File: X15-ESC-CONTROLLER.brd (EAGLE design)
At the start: 51.6 x 34.2 mm, 27 parts, among them IC1 OP-AMP, J1 3V3 -SWCLK-GND-SWDIO- NRST, Y1 ECS-80-S-4X

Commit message: First finished version
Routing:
- net GND: track 161.2 -> 160.6 mm
- net TIM2_CH2: track 37.2 -> 36.6 mm

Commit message: Final Version 2
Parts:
- moved J2 1.07 mm to (19.9, 3.15)
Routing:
- net TIM3_CH3: track 33.8 -> 32.2 mm
- net ADC_IN4: track 23.5 -> 22.0 mm
- net TIM3_CH4: track 35.2 -> 33.9 mm
- net TIM1_CH1: track 41.9 -> 43.1 mm
- net TIM16_CH1: track 37.5 -> 36.5 mm

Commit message: Update Parts Library
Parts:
- D1: device LED, 0805:0805 -> X15-ESC-Controller-Parts-Library:0805
- U$7: device OTHER, Push button - FSM2JMTR:DISCRETECOMPONENTS_SW_2512 -> X15-ESC-Controller-Parts-Library:DISCRETECOMPONENTS_SW_2512
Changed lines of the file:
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@@
 <attribute name="VALUE" x="8.2296" y="10.2108" size="0.6096" layer="28" font="vector" ratio="20" rot="MR180"/>
 </element>
-<element name="U$7" library="OTHER, Push button - FSM2JMTR" package="DISCRETECOMPONENTS_SW_2512" package3d_urn="urn:adsk.eagle:package:24384574/2" value="" x="4.445" y="8.382" smashed="yes" rot="R90">
+<element name="U$7" library="X15-ESC-Controller-Parts-Library" package="DISCRETECOMPONENTS_SW_2512" package3d_urn="urn:adsk.eagle:package:24384574/2" value="" x="4.445" y="8.382" smashed="yes" rot="R90">
 <attribute name="NAME" x="2.54" y="8.382" size="1.27" layer="25" rot="R90" align="bottom-center"/>
 <attribute name="VALUE" x="6.35" y="8.382" size="1.27" layer="27" rot="R90" align="top-center"/>
 </element>
-<element name="D1" library="LED, 0805" package="0805" value="COLOR" x="2.667" y="14.6812" smashed="yes">
+<element name="D1" library="X15-ESC-Controller-Parts-Library" package="0805" value="COLOR" x="2.667" y="14.6812" smashed="yes">
 <attribute name="NAME" x="2.667" y="15.5702" size="0.6096" layer="25" font="vector" ratio="20" align="bottom-center"/>
 <attribute name="VALUE" x="2.667" y="13.7922" size="0.6096" layer="27" font="vector" ratio="20" align="top-center"/>

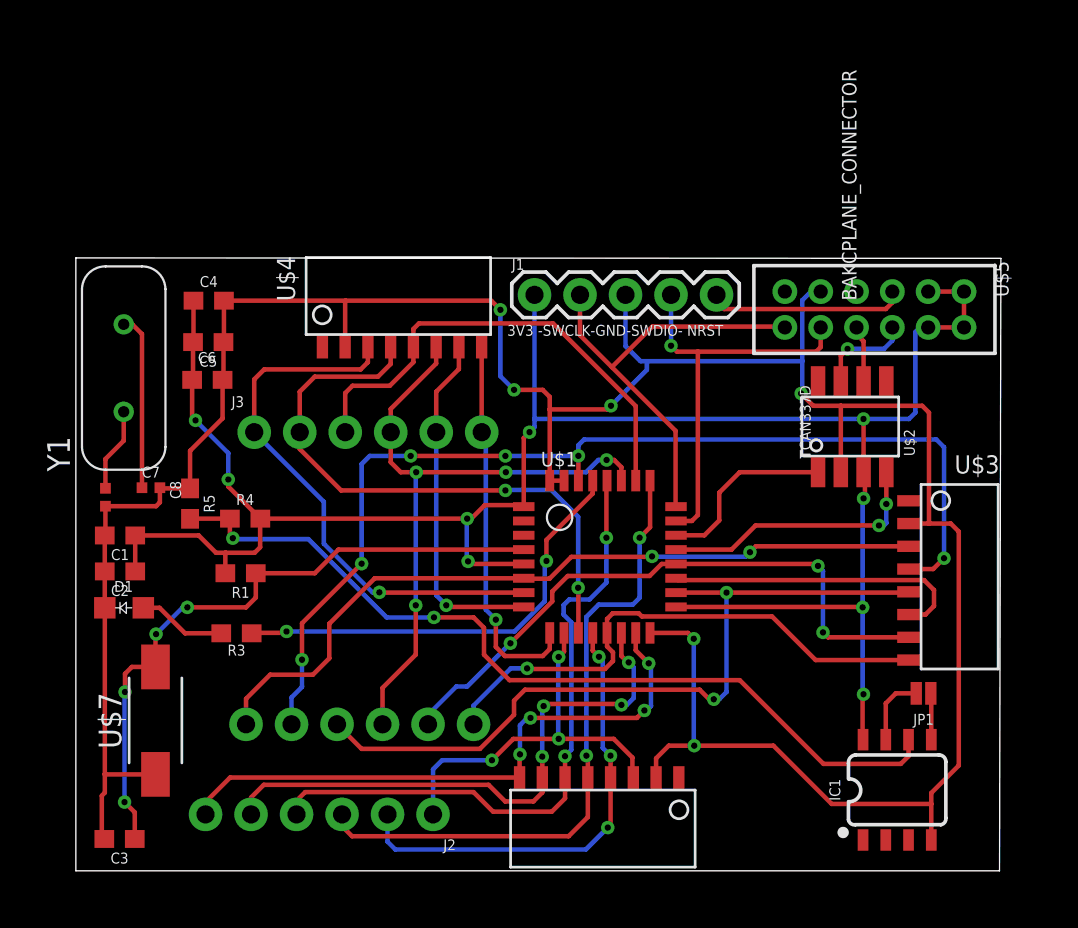
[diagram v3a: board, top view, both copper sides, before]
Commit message: Fix some traces with polygons
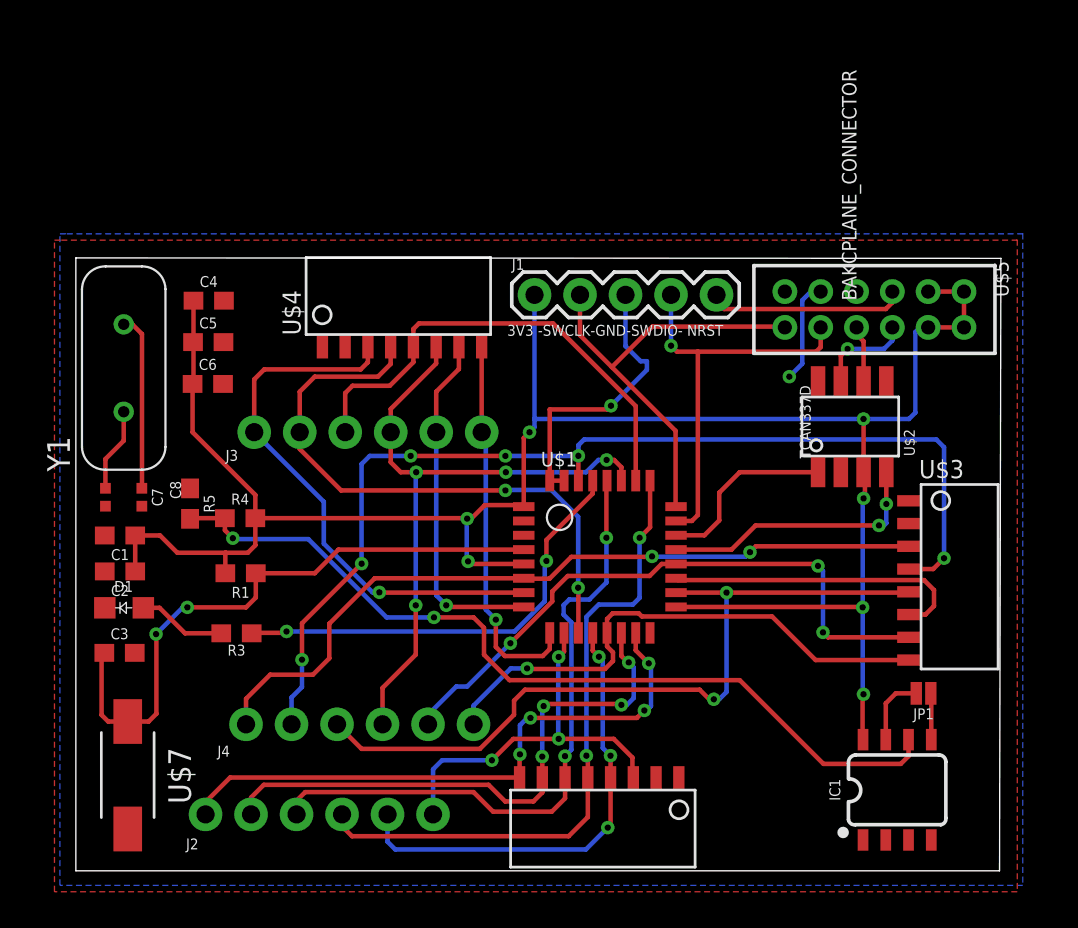
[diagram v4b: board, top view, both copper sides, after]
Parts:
- moved C3 10.4 mm to (2.44, 12.2), turned to 0 degrees
- moved U$7 3.42 mm to (2.90, 5.33)
- moved C7 0.74 mm to (3.68, 20.9), turned to 270 degrees
- moved R4 0.28 mm to (9.17, 19.7)
- moved C6 0.23 mm to (7.37, 27.2)
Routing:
- net GND: track 160.6 -> 21.8 mm, vias 6 -> 2
- net N$2: track 36.4 -> 34.7 mm, vias 4 -> 2
- net +3V3: track 119.9 -> 119.8 mm, vias 9 -> 7
- added copper zone on layer 1, net GND
- added copper zone on layer 16, net GND

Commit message: Add 3.3V testing LED
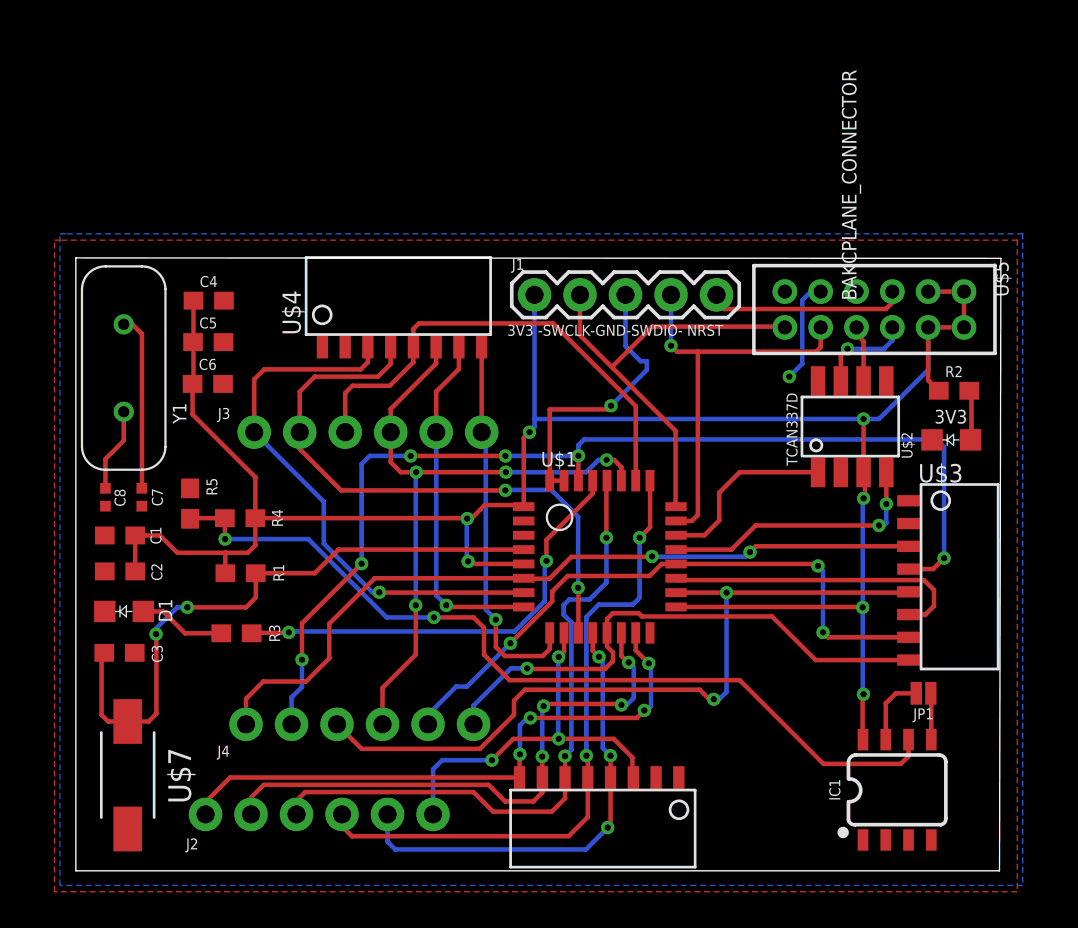
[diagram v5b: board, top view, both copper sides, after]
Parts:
- added 3V3: COLOR, X15-ESC-Controller-Parts-Library:0805
- added R2: 150, SparkFun-Resistors:0603
- moved D1 0.20 mm to (2.67, 14.5)
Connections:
- new net N$1: 3V3.A, R2.2
- net +3V3: now also R2.1
- net GND: now also 3V3.C
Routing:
- net N$1: track 0.00 -> 2.82 mm
- net +3V3: track 119.8 -> 122.3 mm

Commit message: Update .brd file
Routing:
- net GND: track 21.8 -> 11.8 mm
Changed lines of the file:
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@@
 </element>
 <element name="3V3" library="X15-ESC-Controller-Parts-Library" package="0805" value="COLOR" x="48.8442" y="24.0538" smashed="yes">
-<attribute name="NAME" x="48.8442" y="24.9682" size="0.762" layer="25" font="vector" ratio="20" align="bottom-center"/>
+<attribute name="NAME" x="48.8442" y="24.9682" size="0.6096" layer="25" font="vector" ratio="20" align="bottom-center"/>
 <attribute name="VALUE" x="49.8856" y="23.3426" size="0.6096" layer="27" font="vector" ratio="20" align="top-center"/>
 </element>
@@
 <contactref element="D1" pad="C"/>
 <via x="39.8272" y="27.5844" extent="1-16" drill="0.35"/>
-<wire x1="30.6832" y1="32.152" x2="30.6832" y2="29.2862" width="0.254" layer="16"/>
-<wire x1="31.5214" y1="28.448" x2="31.877" y2="28.448" width="0.254" layer="16"/>
-<wire x1="31.5214" y1="28.448" x2="30.6832" y2="29.2862" width="0.254" layer="16"/>
 <wire x1="26.4526" y1="21.7798" x2="27.2526" y2="21.7798" width="0.254" layer="1"/>
-<wire x1="26.4526" y1="25.7556" x2="26.4526" y2="21.7798" width="0.254" layer="1"/>
-<wire x1="26.4526" y1="25.7556" x2="29.6672" y2="25.7556" width="0.254" layer="1"/>
 <wire x1="41.5776" y1="32.3342" x2="41.0346" y2="32.3342" width="0.254" layer="16"/>
 <wire x1="40.552" y1="31.8516" x2="40.552" y2="28.3092" width="0.254" layer="16"/>
 <wire x1="41.0346" y1="32.3342" x2="40.552" y2="31.8516" width="0.254" layer="16"/>
 <wire x1="40.552" y1="28.3092" x2="39.8272" y2="27.5844" width="0.254" layer="16"/>
-<wire x1="31.877" y1="27.9654" x2="31.877" y2="28.448" width="0.254" layer="16"/>
-<wire x1="29.872421875" y1="25.960821875" x2="31.877" y2="27.9654" width="0.254" layer="16"/>
-<wire x1="29.6672" y1="25.7556" x2="29.872421875" y2="25.960821875" width="0.254" layer="1"/>
-<via x="29.872421875" y="25.960821875" extent="1-16" drill="0.35"/>
+<wire x1="26.4526" y1="21.7798" x2="26.4526" y2="26.94224375" width="0.254" layer="1"/>
+<wire x1="26.4526" y1="26.94224375" x2="26.443421875" y2="26.951421875" width="0.254" layer="1"/>
+<via x="26.443421875" y="26.951421875" extent="1-16" drill="0.35"/>
 <polygon width="0.1524" layer="1" isolate="0.2032">
 <vertex x="-0.8128" y="35.2044"/>

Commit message: Complete Board
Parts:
- JP1: value JUMPER-SMT_2_NO_NO-SILK -> JUMPER-SMT
- U$3, U$4, U$6: device X15-ESC-Controller-Parts-Library:JST_8_PIN -> X15-ESC-Controller-Parts-Library:8PIN_CONNECTOR
- moved U$4 10.2 mm to (12.4, 28.4), turned to 0 degrees
- moved U$6 9.39 mm to (34.1, 5.82), turned to 180 degrees
- moved U$3 8.28 mm to (45.8, 20.0), turned to 270 degrees
- moved IC1 7.17 mm to (38.7, 4.70)
- moved JP1 4.88 mm to (42.4, 9.91), turned to 90 degrees
- moved R4 2.27 mm to (7.11, 18.7), turned to 180 degrees
- moved R3 2.22 mm to (7.11, 14.5)
- moved J4 2.21 mm to (7.29, 8.13)
- moved R1 2.09 mm to (7.11, 16.7)
- moved R5 0.83 mm to (7.11, 20.9), turned to 0 degrees
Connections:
- net ADC_IN0: now also U$3.1; no longer U$3.3
- net ADC_IN1: now also U$4.1; no longer U$4.3
- net ADC_IN4: now also U$6.1; no longer U$6.3
- net TIM16_CH1: now also U$6.4; no longer U$6.5
- net TIM17_CH1: now also U$3.7; no longer U$3.8
- net TIM1_CH1: now also U$3.4; no longer U$3.5
- net TIM1_CH2: now also U$3.5; no longer U$3.6
- net TIM1_CH3: now also U$3.6; no longer U$3.7
- net TIM2_CH1: now also U$4.4; no longer U$4.5
- net TIM2_CH2: now also U$4.5; no longer U$4.6
- net TIM2_CH3: now also U$4.6; no longer U$4.7
- net TIM2_CH4: now also U$4.7; no longer U$4.8
- net TIM3_CH2: now also U$6.5; no longer U$6.6
- net TIM3_CH3: now also U$6.6; no longer U$6.7
- net TIM3_CH4: now also U$6.7; no longer U$6.8
- net TLM_1: now also U$3.8; no longer U$3.4
- net TLM_2: now also U$4.8; no longer U$4.4
- net TLM_3: now also U$6.8; no longer U$6.4
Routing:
- net TIM3_CH2: track 36.4 -> 53.2 mm, vias 2 -> 1
- net +3V3: track 122.3 -> 108.9 mm, vias 7 -> 6
- net ADC_IN4: track 22.0 -> 30.4 mm
- net SWDIO: track 23.0 -> 28.6 mm, vias 1 -> 0
- net TLM_2: track 33.5 -> 38.9 mm, vias 2 -> 3
- net N$3: track 48.5 -> 43.4 mm
- net ADC_IN1: track 30.7 -> 26.0 mm
- net TLM_3: track 25.8 -> 21.7 mm, vias 3 -> 2
- net TIM1_CH2: track 17.2 -> 13.3 mm, vias 0 -> 2
- net N$2: track 34.8 -> 38.5 mm
- net N$4: track 24.9 -> 27.9 mm
- net TIM1_CH3: track 34.9 -> 37.7 mm
- net TIM2_CH3: track 19.5 -> 16.8 mm
- net GND: track 11.8 -> 9.24 mm, vias 2 -> 23
- net N$8: track 4.85 -> 2.49 mm
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- added copper zone on layer 1, net +3V3
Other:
- board text added: "X15 ESC-Controller Akhilesh Prasad Derek Chi Minh Nguyen Bryce Sasser Rachel Livesay Katherine Sandys"

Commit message: Fix .brd files
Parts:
- moved C7 1.88 mm to (2.18, 19.7), turned to 180 degrees
- moved C2 0.64 mm to (2.51, 16.1)
- moved C3 0.64 mm to (2.49, 11.5)
- moved R1 0.64 mm to (7.16, 16.1)
- moved D1 0.64 mm to (2.72, 13.8)
- moved R3 0.64 mm to (7.16, 13.8)
- moved C1 0.64 mm to (2.51, 18.1)
- moved R4 0.64 mm to (7.16, 18.1)
- moved R5 0.64 mm to (7.16, 20.2)
- moved C8 0.58 mm to (2.18, 21.1), turned to 180 degrees
- moved JP1 0.23 mm to (42.4, 9.68)
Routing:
- net +3V3: track 108.9 -> 113.9 mm
- net N$6: track 9.86 -> 12.7 mm
- net TLM_2: track 38.9 -> 40.9 mm
- net TLM_1: track 59.9 -> 61.7 mm
- net N$4: track 27.9 -> 29.2 mm
- net ADC_IN0: track 44.7 -> 45.6 mm
- net N$2: track 38.5 -> 37.7 mm
- net TIM3_CH2: track 53.2 -> 52.4 mm
- net ADC_IN1: track 26.0 -> 26.7 mm
- net TIM2_CH2: track 38.8 -> 38.1 mm
- net TIM2_CH3: track 16.8 -> 17.4 mm
- net N$3: track 43.4 -> 42.8 mm
